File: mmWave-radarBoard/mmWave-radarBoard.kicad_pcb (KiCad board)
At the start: 2 copper layers, 1 part, among them U2 XI6432BRQAAMY

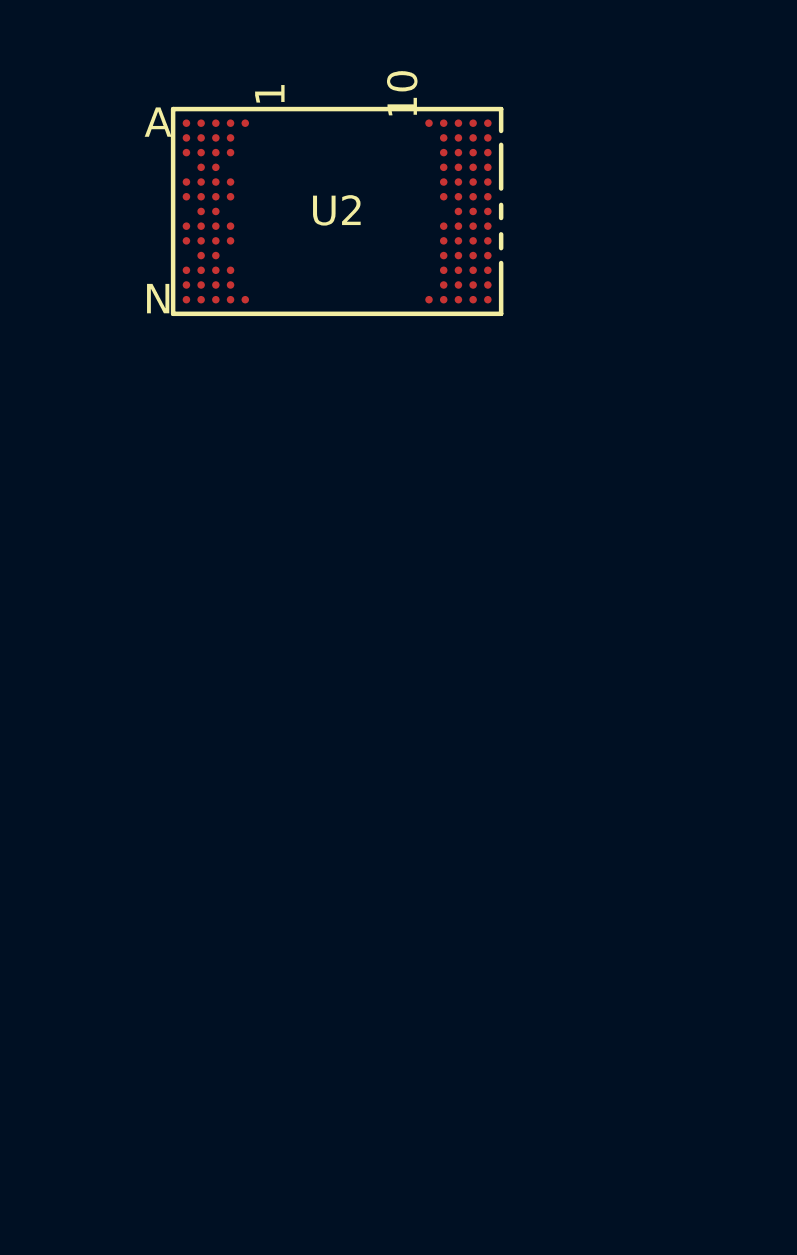
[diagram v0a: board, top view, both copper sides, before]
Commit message: Started working on the schematic
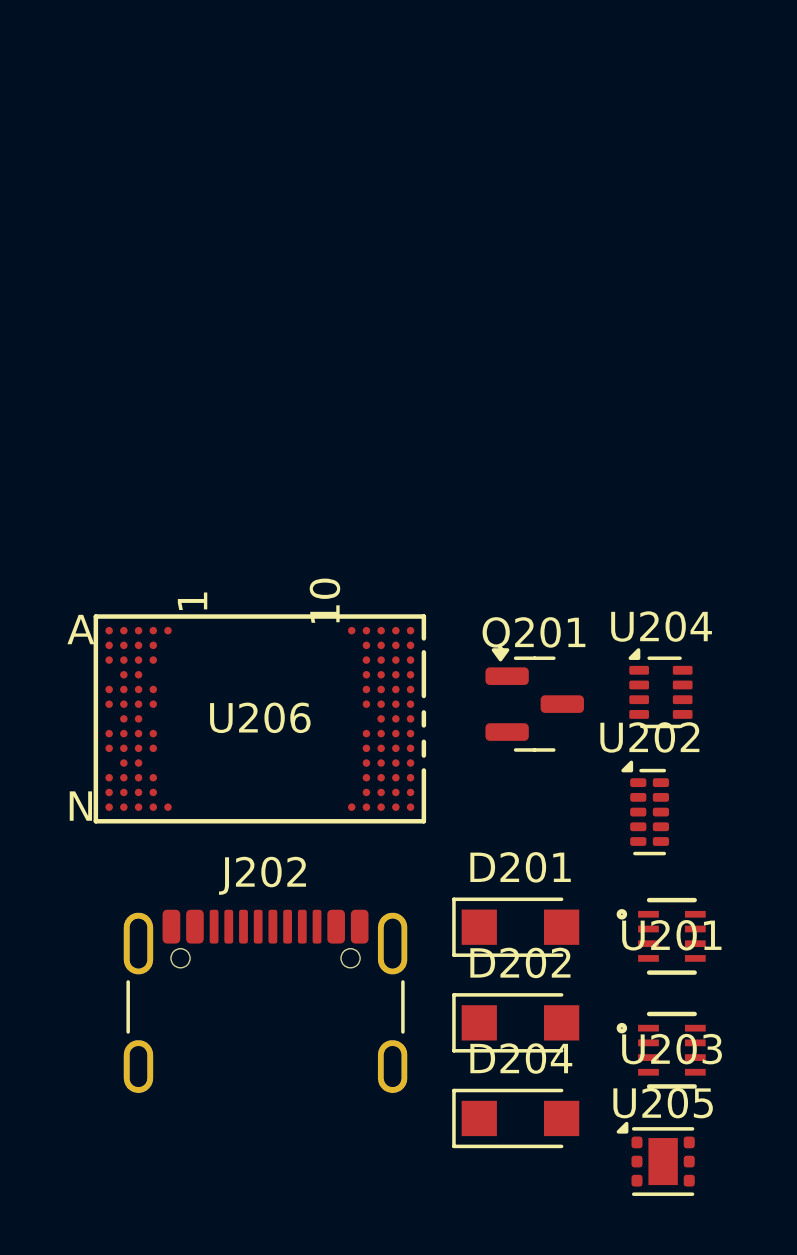
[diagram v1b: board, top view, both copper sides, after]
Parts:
- removed U2: XI6432BRQAAMY, XI6432B:FCCSP101_AMY_TEX
- added D201: PMEG3020ER, Diode_SMD:Nexperia_CFP3_SOD-123W, F.Cu at (152.4, 122.6)
- added D202: PMEG3020ER, Diode_SMD:Nexperia_CFP3_SOD-123W, F.Cu at (152.4, 125.8)
- added D204: PMEG3020ER, Diode_SMD:Nexperia_CFP3_SOD-123W, F.Cu at (152.4, 129.1)
- added J202: USB_C_Receptacle_USB2.0_16P, Connector_USB:USB_C_Receptacle_GCT_USB4105-xx-A_16P_TopMnt_Horizontal, F.Cu at (143.7, 126.2)
- added Q201: BSS123, Package_TO_SOT_SMD:SOT-23, F.Cu at (152.8, 115.0)
- added U201: TPS628502DRLR, TPS62850x:SOT-5X3-8_DRL_TEX, F.Cu at (157.5, 122.9)
- added U202: TPD4EUSB30, Package_SON:USON-10_2.5x1.0mm_P0.5mm, F.Cu at (156.7, 118.7)
- added U203: TPS628502DRLR, TPS62850x:SOT-5X3-8_DRL_TEX, F.Cu at (157.5, 126.8)
- added U204: TPS2116DRL, Package_TO_SOT_SMD:SOT-583-8, F.Cu at (157.1, 114.6)
- added U205: TLV75533PDRV, Package_SON:WSON-6-1EP_2x2mm_P0.65mm_EP1x1.6mm, F.Cu at (157.2, 130.5)
- added U206: XI6432BRQAAMY, XI6432B:FCCSP101_AMY_TEX, F.Cu at (143.5, 115.5)

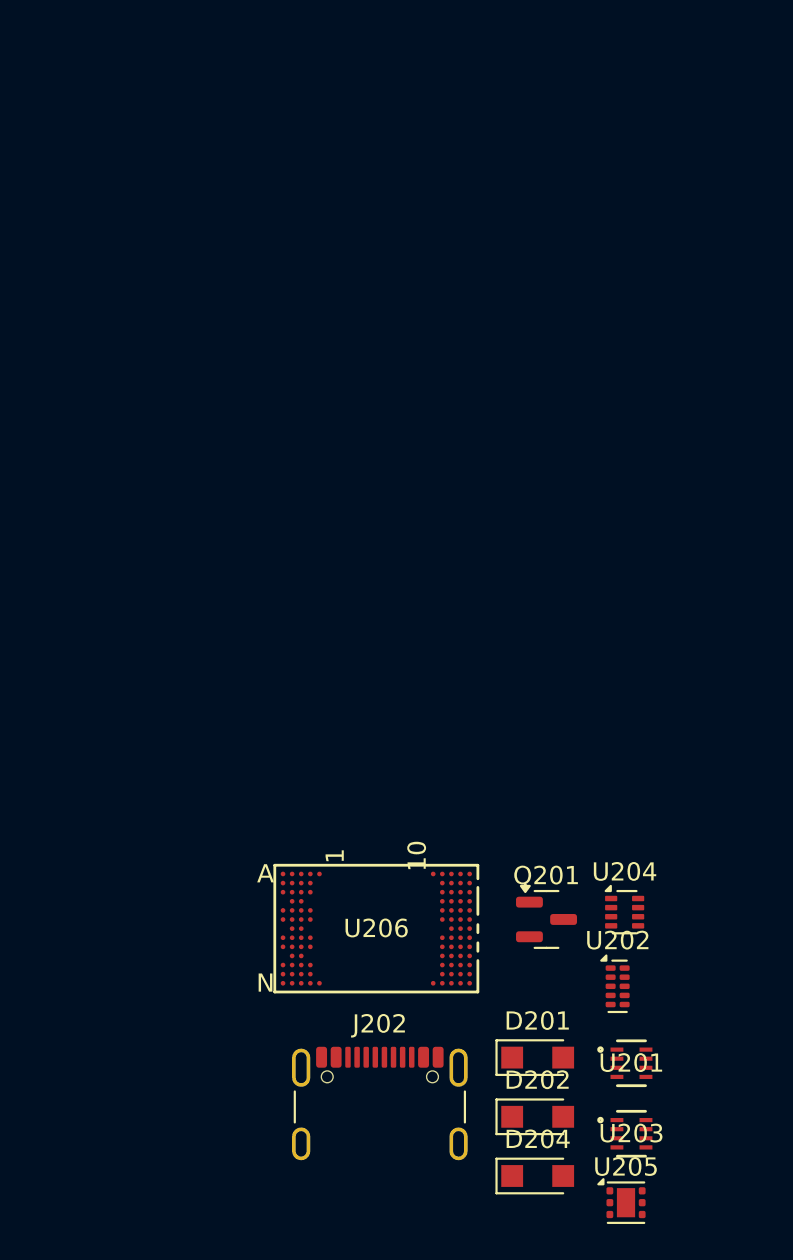
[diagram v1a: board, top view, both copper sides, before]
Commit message: Updated schematic of the radar module
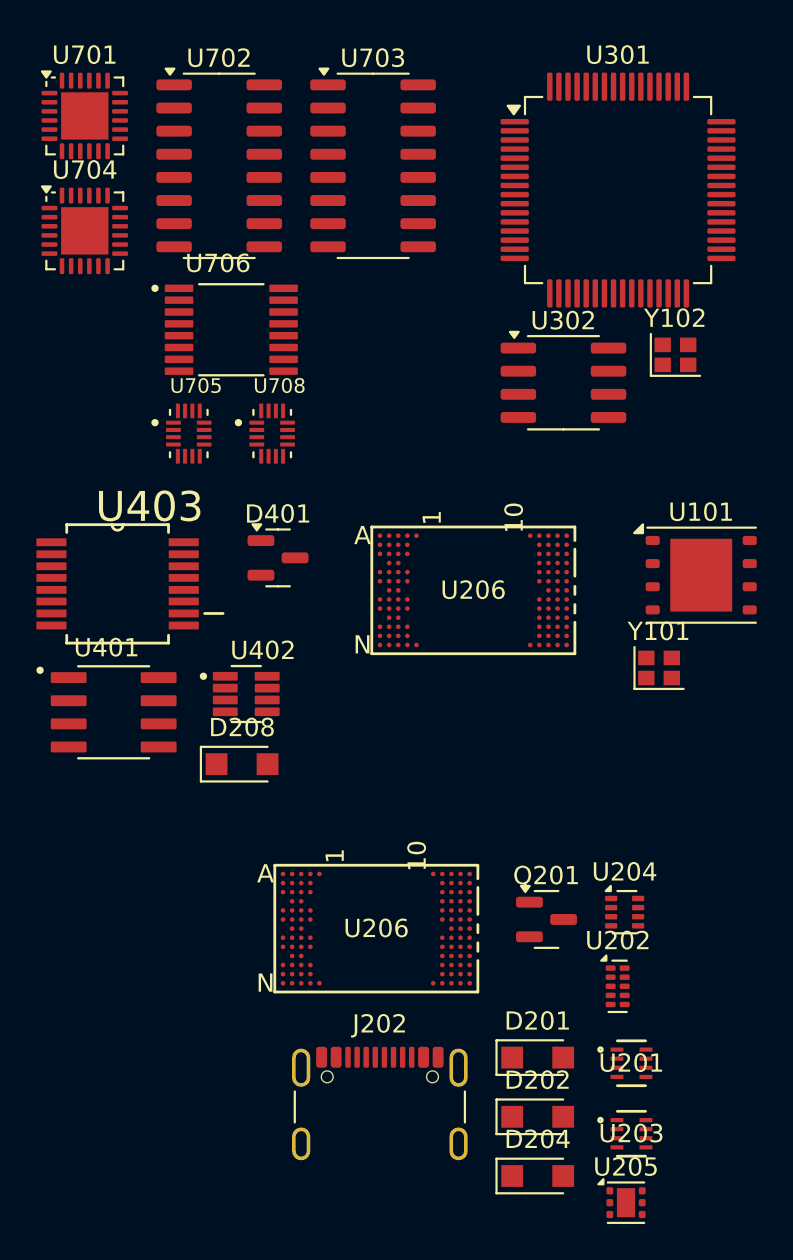
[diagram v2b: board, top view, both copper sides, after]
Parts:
- added D208: PMEG3020ER, Diode_SMD:Nexperia_CFP3_SOD-123W, F.Cu at (136.1, 106.5)
- added D401: NUP2105L, Package_TO_SOT_SMD:SOT-23, F.Cu at (138.1, 95.1)
- added U101: MX25R1635FZUIH0, Package_SON:WSON-8-1EP_6x5mm_P1.27mm_EP3.4x4mm, F.Cu at (161.3, 96.1)
- added U206: XI6432BRQAAMY, XI6432B:FCCSP101_AMY_TEX, F.Cu at (148.8, 96.9)
- added U301: FT4232H, Package_QFP:LQFP-64_10x10mm_P0.5mm, F.Cu at (156.8, 75.0)
- added U302: 93LCxxB, Package_SO:SOIC-8_3.9x4.9mm_P1.27mm, F.Cu at (153.8, 85.5)
- added U401: TCAN1042HGVDRQ1, TCAN1042HGVDRQ1:SOIC127P599X175-8N, F.Cu at (129.1, 103.6)
- added U402: TLIN1039DDFRQ1, TLIN1039DDFRQ1:SOT65P280X110-8N, F.Cu at (136.4, 102.6)
- added U403: TRS3221EIDBR, TRS3221EIDBR:SOP65P780X200-16N, F.Cu at (129.3, 96.6)
- added U701: TS3A27518ERTW, Package_DFN_QFN:WQFN-24-1EP_4x4mm_P0.5mm_EP2.6x2.6mm, F.Cu at (127.5, 70.9)
- added U702: SN65LVDS047D, Package_SO:SOIC-16_3.9x9.9mm_P1.27mm, F.Cu at (134.9, 73.6)
- added U703: SN65LVDS047D, Package_SO:SOIC-16_3.9x9.9mm_P1.27mm, F.Cu at (143.3, 73.6)
- added U704: TS3A27518ERTW, Package_DFN_QFN:WQFN-24-1EP_4x4mm_P0.5mm_EP2.6x2.6mm, F.Cu at (127.5, 77.2)
- added U705: TS3A5018RSVR, TS3A5018RSVR:QFN40P260X180X55-16N, F.Cu at (133.2, 88.3)
- added U706: TS3A44159PWR, TS3A44159PWR:SOP65P640X120-16N, F.Cu at (135.5, 82.6)
- added U708: TS3A5018RSVR, TS3A5018RSVR:QFN40P260X180X55-16N, F.Cu at (137.8, 88.3)
- added Y101: 40MHz, Crystal:Crystal_SMD_2016-4Pin_2.0x1.6mm, F.Cu at (159.0, 101.2)
- added Y102: 12MHz, Crystal:Crystal_SMD_2016-4Pin_2.0x1.6mm, F.Cu at (159.9, 84.0)
